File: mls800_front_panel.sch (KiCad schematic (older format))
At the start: 17 parts, among them P5 CONN_02X03, SW10 SW_TACT_LED, SW11 SW_TACT_LED, SW2 SW_TACT_LED, SW3 SW_TACT_LED, SW4 SW_TACT_LED, SW5 SW_TACT_LED, SW6 SW_TACT_LED, SW7 SW_TACT_LED, SW8 SW_TACT_LED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

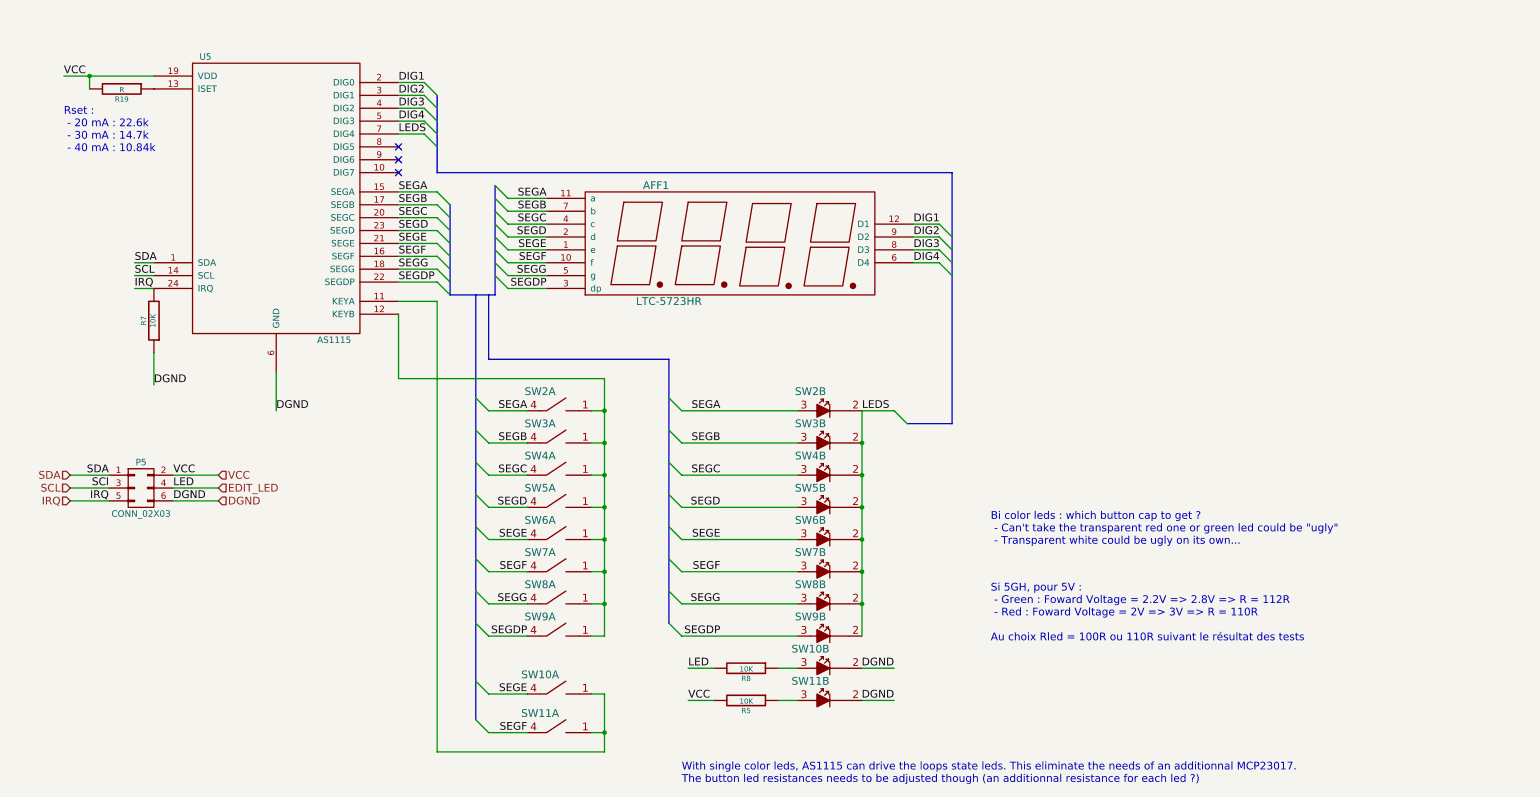
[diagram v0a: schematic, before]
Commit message: MLS800
* splitted schematics for DRC tests
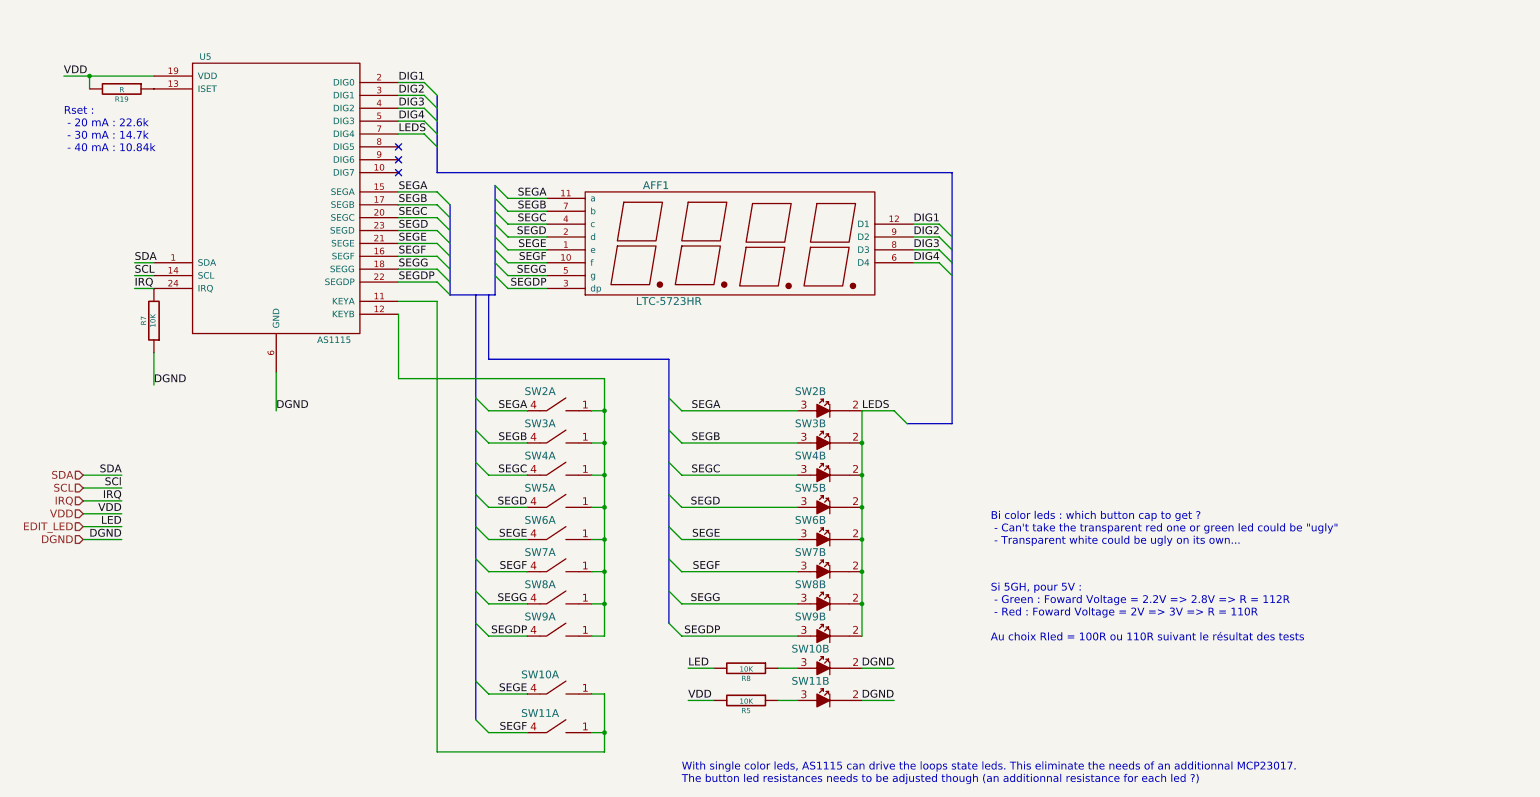
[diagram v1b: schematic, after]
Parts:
- removed P5: CONN_02X03, Pin_Headers:Pin_Header_Straight_2x03, symbol CONN_02X03
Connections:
- net VCC renamed VDD
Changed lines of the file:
@@
 	-1   0    0    1
 $EndComp
-$Comp
-L CONN_02X03 P5
-U 1 1 5497CC76
-P 1450 4150
-F 0 "P5" H 1450 4350 50  0000 C CNN
-F 1 "CONN_02X03" H 1450 3950 50  0000 C CNN
-F 2 "Pin_Headers:Pin_Header_Straight_2x03" H 1450 2950 60  0001 C CNN
-F 3 "" H 1450 2950 60  0000 C CNN
-	1    1450 4150
-	1    0    0    -1
-$EndComp
-Text HLabel 900  4050 0    60   Input ~ 0
-SDA
-Text HLabel 2050 4050 2    60   Input ~ 0
-VCC
-Text HLabel 2050 4250 2    60   Input ~ 0
-DGND
-Text HLabel 2050 4150 2    60   Input ~ 0
-EDIT_LED
-Text HLabel 900  4250 0    60   Input ~ 0
-IRQ
-Text HLabel 900  4150 0    60   Input ~ 0
-SCL
 Wire Wire Line
 	3650 1000 3450 1000
@@
 Wire Wire Line
 	1400 2600 1550 2600
-Wire Wire Line
-	1200 4050 900  4050
-Wire Wire Line
-	900  4150 1200 4150
-Wire Wire Line
-	900  4250 1200 4250
-Wire Wire Line
-	2050 4050 1700 4050
-Wire Wire Line
-	1700 4150 2050 4150
-Wire Wire Line
-	1700 4250 2050 4250
-Text Label 1700 4050 0    60   ~ 0
-VCC
-Text Label 1700 4150 0    60   ~ 0
-LED
-Text Label 1700 4250 0    60   ~ 0
-DGND
-Text Label 1200 4050 2    60   ~ 0
-SDA
-Text Label 1200 4150 2    60   ~ 0
-SCl
-Text Label 1200 4250 2    60   ~ 0
-IRQ
 Connection ~ 1050 950
 Text Label 850  950  0    60   ~ 0
-VCC
+VDD
 Wire Wire Line
 	2500 3250 2500 3550
@@
 	5900 5800 5700 5800
 Text Label 5700 5800 0    60   ~ 0
-VCC
+VDD
 Wire Wire Line
 	7050 5550 7300 5550
@@
 Text Label 7300 5550 2    60   ~ 0
 DGND
+Text Label 1300 4250 2    60   ~ 0
+IRQ
+Text Label 1300 4150 2    60   ~ 0
+SCl
+Text Label 1300 4050 2    60   ~ 0
+SDA
+Text Label 1300 4550 2    60   ~ 0
+DGND
+Text Label 1300 4450 2    60   ~ 0
+LED
+Text Label 1300 4350 2    60   ~ 0
+VDD
+Wire Wire Line
+	1300 4550 1000 4550
+Wire Wire Line
+	1300 4450 1000 4450
+Wire Wire Line
+	1000 4350 1300 4350
+Wire Wire Line
+	1000 4250 1300 4250
+Wire Wire Line
+	1000 4150 1300 4150
+Wire Wire Line
+	1300 4050 1000 4050
+Text HLabel 1000 4150 0    60   Input ~ 0
+SCL
+Text HLabel 1000 4250 0    60   Input ~ 0
+IRQ
+Text HLabel 1000 4450 0    60   Input ~ 0
+EDIT_LED
+Text HLabel 1000 4550 0    60   Input ~ 0
+DGND
+Text HLabel 1000 4350 0    60   Input ~ 0
+VDD
+Text HLabel 1000 4050 0    60   Input ~ 0
+SDA
 $EndSCHEMATC

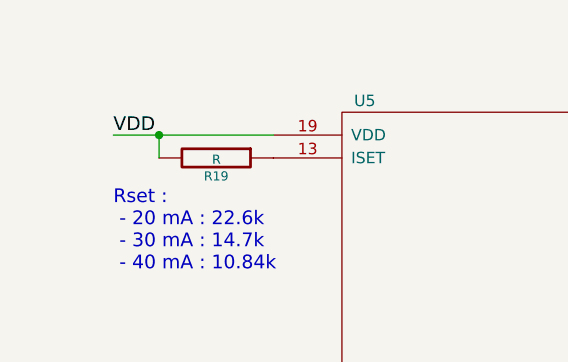
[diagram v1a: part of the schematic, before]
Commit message: MLS800
* rerouting of some part
* added filter cap to each digital part
* added board filter cap
* set 3d shapes for remaining parts (missing custom parts)
* added footprint for small pushbutton
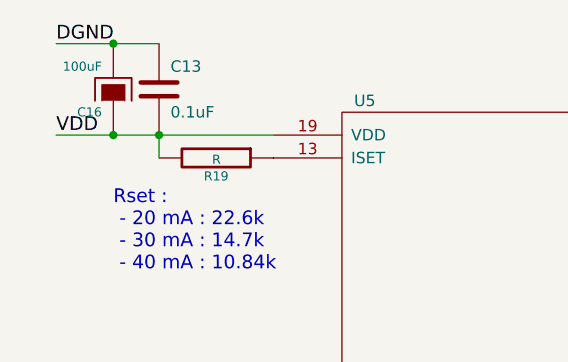
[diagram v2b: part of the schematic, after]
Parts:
- added C13: 0.1uF, Capacitors_SMD:C_0805_HandSoldering, symbol C
- added C16: 100uF, Capacitors_SMD:C_0805_HandSoldering, symbol CAPAPOL
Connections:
- net DGND: now also C13.1, C16.2
- net VDD: now also C13.2, C16.1
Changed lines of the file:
@@
 	1050 1050 1050 950
 Wire Wire Line
-	850  950  1550 950
+	600  950  1550 950
 Wire Wire Line
 	4450 5300 4150 5300
@@
 	1400 2600 1550 2600
 Connection ~ 1050 950
-Text Label 850  950  0    60   ~ 0
+Text Label 600  950  0    60   ~ 0
 VDD
 Wire Wire Line
@@
 Text HLabel 1000 4050 0    60   Input ~ 0
 SDA
+$Comp
+L C C13
+U 1 1 54D9EF4F
+P 1050 750
+F 0 "C13" H 1100 850 50  0000 L CNN
+F 1 "0.1uF" H 1100 650 50  0000 L CNN
+F 2 "Capacitors_SMD:C_0805_HandSoldering" H 1088 600 30  0001 C CNN
+F 3 "" H 1050 750 60  0000 C CNN
+	1    1050 750
+	1    0    0    -1
+$EndComp
+Wire Wire Line
+	600  550  1050 550
+Text Label 600  550  0    60   ~ 0
+DGND
+$Comp
+L CAPAPOL C16
+U 1 1 54DC240E
+P 850 750
+F 0 "C16" H 900 850 40  0000 L CNN
+F 1 "100uF" H 900 650 40  0000 L CNN
+F 2 "Capacitors_SMD:C_0805_HandSoldering" H 950 600 30  0001 C CNN
+F 3 "" H 850 750 300 0000 C CNN
+	1    850  750
+	-1   0    0    1
+$EndComp
+Connection ~ 850  550
+Connection ~ 850  950
 $EndSCHEMATC

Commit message: MLS800
* copper zone clearance
* round drilling holes
*
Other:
- note added: "If using 5V for 5GH : \n - Green : Foward Voltage = 2.2V => 2.8V => R = 112R\n - Red : Foward Voltage = 2V => 3V => R = 110R\n\nAu choix Rled = 100R ou 110R suivant le résultat des tests"
- note removed: "Si 5GH, pour 5V : \n - Green : Foward Voltage = 2.2V => 2.8V => R = 112R\n - Red : Foward Voltage = 2V => 3V => R = 110R\n\nAu choix Rled = 100R ou 110R suivant le résultat des tests"
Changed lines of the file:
@@
 encoding utf-8
 Sheet 3 3
-Title ""
-Date ""
-Rev ""
+Title "MLS800 prototype"
+Date "mercredi 18 février 2015"
+Rev "B"
 Comp ""
 Comment1 ""
@@
 NoConn ~ 3450 1700
 Text Notes 8050 5350 0    60   ~ 0
-Si 5GH, pour 5V : \n - Green : Foward Voltage = 2.2V => 2.8V => R = 112R\n - Red : Foward Voltage = 2V => 3V => R = 110R\n\nAu choix Rled = 100R ou 110R suivant le résultat des tests
+If using 5V for 5GH : \n - Green : Foward Voltage = 2.2V => 2.8V => R = 112R\n - Red : Foward Voltage = 2V => 3V => R = 110R\n\nAu choix Rled = 100R ou 110R suivant le résultat des tests
 $Comp
 L SW_TACT_LED SW10

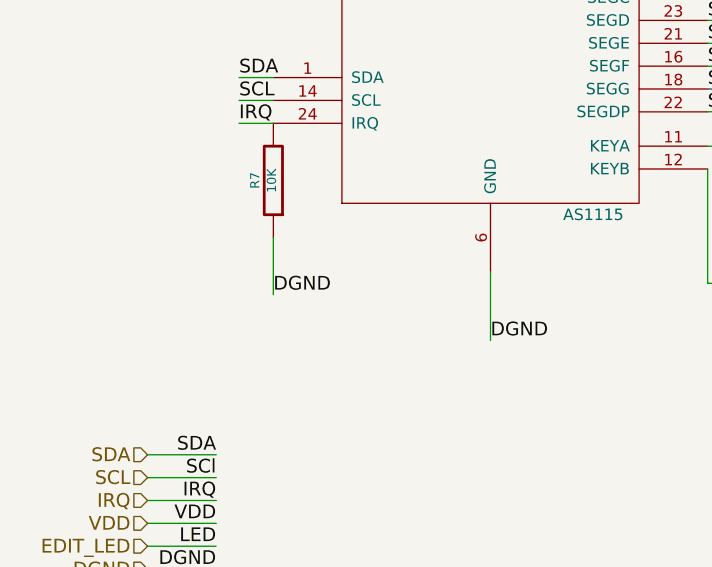
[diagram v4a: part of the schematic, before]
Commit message: Minor PCB adjustements
Fixed R7 tied to ground instead of VCC (needs to be reported on PCB)
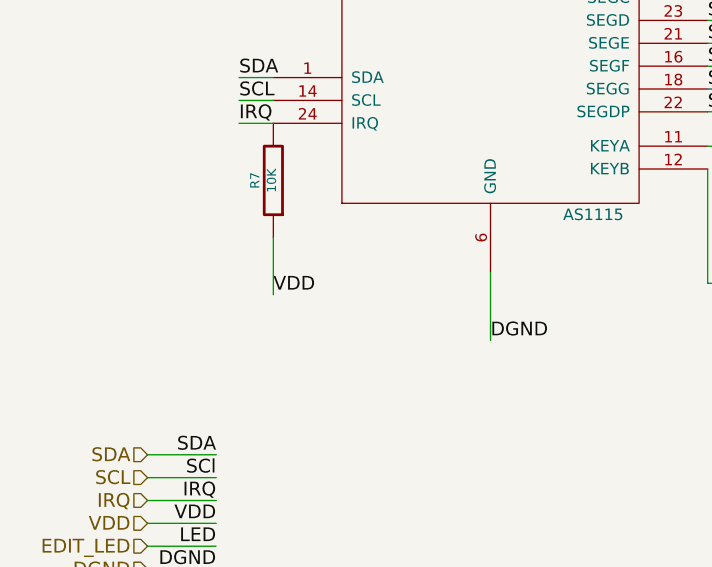
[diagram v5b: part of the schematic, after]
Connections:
- net DGND: no longer R7.1
- net VDD: now also R7.1
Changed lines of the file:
@@
 Text Label 2500 3550 0    60   ~ 0
-DGND
-Text Label 1550 3350 0    60   ~ 0
 DGND
 Wire Wire Line
@@
 Connection ~ 850  550
 Connection ~ 850  950
+Text Label 1550 3350 0    60   ~ 0
+VDD
 $EndSCHEMATC

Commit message: Started components fields assignments
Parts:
- AFF1: Manufacturer (none) -> Lite-On; Manufacturer part number (none) -> LTC-5723HR
- U5: Manufacturer (none) -> ams AG; Manufacturer part number (none) -> AS1115-BSST; Package (none) -> TQFN-24
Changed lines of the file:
@@
 F 2 "Custom-display:LTC-5723" H 5550 2250 60  0001 C CNN
 F 3 "" H 5550 2250 60  0000 C CNN
+F 4 "Lite-On" H 6050 2250 60  0001 C CNN "Manufacturer"
+F 5 "LTC-5723HR" H 6050 2250 60  0001 C CNN "Manufacturer part number"
 	1    6050 2250
 	1    0    0    -1
@@
 F 2 "Housings_SSOP:SSOP-24_3.9x8.7mm_Pitch0.635mm" H 2000 800 50  0001 C CNN
 F 3 "" H 2500 1850 50  0001 C CNN
+F 4 "ams AG" H 2500 1900 60  0001 C CNN "Manufacturer"
+F 5 "AS1115-BSST" H 2500 1900 60  0001 C CNN "Manufacturer part number"
+F 6 "TQFN-24" H 2500 1900 60  0001 C CNN "Package"
 	1    2500 1900
 	1    0    0    -1

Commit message: Components fields assignments
Rerouted relays (set/reset was wired the same way, to reset would have no effect)
Set and reset port have been exchanged to facilitate routing (to be reported on firmware)
Edited relay component
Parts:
- C13, R19, R5, R7, R8: Package (none) -> 0805
- C16: symbol CAPAPOL -> C; Package (none) -> 0805
- SW10, SW11, SW2, SW3, SW5, SW6, SW7, SW8, SW9: Manufacturer (none) -> MEC switches; Manufacturer part number (none) -> 5GSH93582
- SW10, SW11, SW2, SW3, SW4, SW5, SW6, SW7, SW8, SW9: Manufacturer (none) -> MEC switches; Manufacturer part number (none) -> 1ES098
- SW4: Manufacturer (none) -> MEC switches
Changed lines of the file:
@@
 F 2 "Resistors_SMD:R_0805_HandSoldering" V 1230 1050 30  0001 C CNN
 F 3 "" H 1300 1050 30  0000 C CNN
+F 4 "0805" V 1300 1050 60  0001 C CNN "Package"
 	1    1300 1050
 	0    1    1    0
@@
 F 2 "Custom-device:MEC-5G" H 4750 3550 60  0001 C CNN
 F 3 "" H 4750 3550 60  0000 C CNN
+F 4 "MEC switches" H 4750 3550 60  0001 C CNN "Manufacturer"
+F 5 "5GSH93582" H 4750 3550 60  0001 C CNN "Manufacturer part number"
 	1    4750 3550
 	1    0    0    -1
@@
 F 2 "Custom-device:MEC-5G" H 4750 3800 60  0001 C CNN
 F 3 "" H 4750 3800 60  0000 C CNN
+F 4 "MEC switches" H 4750 3800 60  0001 C CNN "Manufacturer"
+F 5 "5GSH93582" H 4750 3800 60  0001 C CNN "Manufacturer part number"
 	1    4750 3800
 	1    0    0    -1
@@
 F 2 "Custom-device:MEC-5G" H 4750 4050 60  0001 C CNN
 F 3 "" H 4750 4050 60  0000 C CNN
+F 4 "MEC switches" H 4750 4050 60  0001 C CNN "Manufacturer"
 	1    4750 4050
 	1    0    0    -1
@@
 F 2 "Custom-device:MEC-5G" H 4750 4300 60  0001 C CNN
 F 3 "" H 4750 4300 60  0000 C CNN
+F 4 "MEC switches" H 4750 4300 60  0001 C CNN "Manufacturer"
+F 5 "5GSH93582" H 4750 4300 60  0001 C CNN "Manufacturer part number"
 	1    4750 4300
 	1    0    0    -1
@@
 F 2 "Custom-device:MEC-5G" H 4750 4550 60  0001 C CNN
 F 3 "" H 4750 4550 60  0000 C CNN
+F 4 "MEC switches" H 4750 4550 60  0001 C CNN "Manufacturer"
+F 5 "5GSH93582" H 4750 4550 60  0001 C CNN "Manufacturer part number"
 	1    4750 4550
 	1    0    0    -1
@@
 F 2 "Custom-device:MEC-5G" H 4750 4800 60  0001 C CNN
 F 3 "" H 4750 4800 60  0000 C CNN
+F 4 "MEC switches" H 4750 4800 60  0001 C CNN "Manufacturer"
+F 5 "5GSH93582" H 4750 4800 60  0001 C CNN "Manufacturer part number"
 	1    4750 4800
 	1    0    0    -1
@@
 F 2 "Custom-device:MEC-5G" H 4750 5050 60  0001 C CNN
 F 3 "" H 4750 5050 60  0000 C CNN
+F 4 "MEC switches" H 4750 5050 60  0001 C CNN "Manufacturer"
+F 5 "5GSH93582" H 4750 5050 60  0001 C CNN "Manufacturer part number"
 	1    4750 5050
 	1    0    0    -1
@@
 F 2 "Custom-device:MEC-5G" H 4750 5300 60  0001 C CNN
 F 3 "" H 4750 5300 60  0000 C CNN
+F 4 "MEC switches" H 4750 5300 60  0001 C CNN "Manufacturer"
+F 5 "5GSH93582" H 4750 5300 60  0001 C CNN "Manufacturer part number"
 	1    4750 5300
 	1    0    0    -1
@@
 F 2 "Custom-device:MEC-5G" H 6850 3550 60  0001 C CNN
 F 3 "" H 6850 3550 60  0000 C CNN
+F 4 "MEC switches" H 6850 3550 60  0001 C CNN "Manufacturer"
+F 5 "1ES098" H 6850 3550 60  0001 C CNN "Manufacturer part number"
 	2    6850 3550
 	1    0    0    -1
@@
 F 2 "Custom-device:MEC-5G" H 6850 3800 60  0001 C CNN
 F 3 "" H 6850 3800 60  0000 C CNN
+F 4 "MEC switches" H 6850 3800 60  0001 C CNN "Manufacturer"
+F 5 "1ES098" H 6850 3800 60  0001 C CNN "Manufacturer part number"
 	2    6850 3800
 	1    0    0    -1
@@
 F 2 "Custom-device:MEC-5G" H 6850 4050 60  0001 C CNN
 F 3 "" H 6850 4050 60  0000 C CNN
+F 4 "MEC switches" H 6850 4050 60  0001 C CNN "Manufacturer"
+F 5 "1ES098" H 6850 4050 60  0001 C CNN "Manufacturer part number"
 	2    6850 4050
 	1    0    0    -1
@@
 F 2 "Custom-device:MEC-5G" H 6850 4300 60  0001 C CNN
 F 3 "" H 6850 4300 60  0000 C CNN
+F 4 "MEC switches" H 6850 4300 60  0001 C CNN "Manufacturer"
+F 5 "1ES098" H 6850 4300 60  0001 C CNN "Manufacturer part number"
 	2    6850 4300
 	1    0    0    -1
@@
 F 2 "Custom-device:MEC-5G" H 6850 4550 60  0001 C CNN
 F 3 "" H 6850 4550 60  0000 C CNN
+F 4 "MEC switches" H 6850 4550 60  0001 C CNN "Manufacturer"
+F 5 "1ES098" H 6850 4550 60  0001 C CNN "Manufacturer part number"
 	2    6850 4550
 	1    0    0    -1
@@
 F 2 "Custom-device:MEC-5G" H 6850 4800 60  0001 C CNN
 F 3 "" H 6850 4800 60  0000 C CNN
+F 4 "MEC switches" H 6850 4800 60  0001 C CNN "Manufacturer"
+F 5 "1ES098" H 6850 4800 60  0001 C CNN "Manufacturer part number"
 	2    6850 4800
 	1    0    0    -1
@@
 F 2 "Custom-device:MEC-5G" H 6850 5050 60  0001 C CNN
 F 3 "" H 6850 5050 60  0000 C CNN
+F 4 "MEC switches" H 6850 5050 60  0001 C CNN "Manufacturer"
+F 5 "1ES098" H 6850 5050 60  0001 C CNN "Manufacturer part number"
 	2    6850 5050
 	1    0    0    -1
@@
 F 2 "Custom-device:MEC-5G" H 6850 5300 60  0001 C CNN
 F 3 "" H 6850 5300 60  0000 C CNN
+F 4 "MEC switches" H 6850 5300 60  0001 C CNN "Manufacturer"
+F 5 "1ES098" H 6850 5300 60  0001 C CNN "Manufacturer part number"
 	2    6850 5300
 	1    0    0    -1
@@
 F 2 "Custom-device:MEC-5G" H 4750 5750 60  0001 C CNN
 F 3 "" H 4750 5750 60  0000 C CNN
+F 4 "MEC switches" H 4750 5750 60  0001 C CNN "Manufacturer"
+F 5 "5GSH93582" H 4750 5750 60  0001 C CNN "Manufacturer part number"
 	1    4750 5750
 	1    0    0    -1
@@
 F 2 "Custom-device:MEC-5G" H 4750 6050 60  0001 C CNN
 F 3 "" H 4750 6050 60  0000 C CNN
+F 4 "MEC switches" H 4750 6050 60  0001 C CNN "Manufacturer"
+F 5 "5GSH93582" H 4750 6050 60  0001 C CNN "Manufacturer part number"
 	1    4750 6050
 	1    0    0    -1
@@
 F 2 "Resistors_SMD:R_0805_HandSoldering" H 6080 5550 30  0001 C CNN
 F 3 "" H 6150 5550 30  0000 C CNN
+F 4 "0805" V 6150 5550 60  0001 C CNN "Package"
 	1    6150 5550
 	0    1    1    0
@@
 F 2 "Custom-device:MEC-5G" H 6850 5550 60  0001 C CNN
 F 3 "" H 6850 5550 60  0000 C CNN
+F 4 "MEC switches" H 6850 5550 60  0001 C CNN "Manufacturer"
+F 5 "1ES098" H 6850 5550 60  0001 C CNN "Manufacturer part number"
 	2    6850 5550
 	1    0    0    -1
@@
 F 2 "Resistors_SMD:R_0805_HandSoldering" H 6080 5800 30  0001 C CNN
 F 3 "" H 6150 5800 30  0000 C CNN
+F 4 "0805" V 6150 5800 60  0001 C CNN "Package"
 	1    6150 5800
 	0    1    1    0
@@
 F 2 "Custom-device:MEC-5G" H 6850 5800 60  0001 C CNN
 F 3 "" H 6850 5800 60  0000 C CNN
+F 4 "MEC switches" H 6850 5800 60  0001 C CNN "Manufacturer"
+F 5 "1ES098" H 6850 5800 60  0001 C CNN "Manufacturer part number"
 	2    6850 5800
 	1    0    0    -1
@@
 F 2 "Resistors_SMD:R_0805_HandSoldering" V 1480 2850 30  0001 C CNN
 F 3 "" H 1550 2850 30  0000 C CNN
+F 4 "0805" V 1550 2850 60  0001 C CNN "Package"
 	1    1550 2850
 	-1   0    0    1
@@
 F 2 "Capacitors_SMD:C_0805_HandSoldering" H 1088 600 30  0001 C CNN
 F 3 "" H 1050 750 60  0000 C CNN
+F 4 "0805" H 1050 750 60  0001 C CNN "Package"
 	1    1050 750
 	1    0    0    -1
@@
 DGND
 $Comp
-L CAPAPOL C16
+L C C16
 U 1 1 54DC240E
 P 850 750
@@
 F 2 "Capacitors_SMD:C_0805_HandSoldering" H 950 600 30  0001 C CNN
 F 3 "" H 850 750 300 0000 C CNN
+F 4 "0805" H 850 750 60  0001 C CNN "Package"
 	1    850  750
 	-1   0    0    1

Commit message: Components fields assignments
Silkscreen dots marker
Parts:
- R19: value R -> 23.6k
- R5, R8: value 10K -> 250R
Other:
- note added: "Rset : \n - 20 mA : 23.6k\n - 30 mA : 15.4k\n - 40 mA : 11.35k"
- note removed: "Bi color leds : which button cap to get ?\n - Can't take the transparent red one or green led could be "ugly"\n - Transparent white could be ugly on its own..."
- note removed: "Rset : \n - 20 mA : 22.6k\n - 30 mA : 14.7k\n - 40 mA : 10.84k"
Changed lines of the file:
@@
 P 1300 1050
 F 0 "R19" V 1380 1050 40  0000 C CNN
-F 1 "R" V 1307 1051 40  0000 C CNN
+F 1 "23.6k" V 1307 1051 40  0000 C CNN
 F 2 "Resistors_SMD:R_0805_HandSoldering" V 1230 1050 30  0001 C CNN
 F 3 "" H 1300 1050 30  0000 C CNN
@@
 $EndComp
 Text Notes 850  1550 0    60   ~ 0
-Rset : \n - 20 mA : 22.6k\n - 30 mA : 14.7k\n - 40 mA : 10.84k
-Text Notes 8050 4600 0    60   ~ 0
-Bi color leds : which button cap to get ?\n - Can't take the transparent red one or green led could be "ugly"\n - Transparent white could be ugly on its own...
+Rset : \n - 20 mA : 23.6k\n - 30 mA : 15.4k\n - 40 mA : 11.35k
 Text Notes 5650 6450 0    60   ~ 0
 With single color leds, AS1115 can drive the loops state leds. This eliminate the needs of an additionnal MCP23017.\nThe button led resistances needs to be adjusted though (an additionnal resistance for each led ?)
@@
 P 6150 5550
 F 0 "R8" V 6230 5550 40  0000 C CNN
-F 1 "10K" V 6157 5551 40  0000 C CNN
+F 1 "250R" V 6157 5551 40  0000 C CNN
 F 2 "Resistors_SMD:R_0805_HandSoldering" H 6080 5550 30  0001 C CNN
 F 3 "" H 6150 5550 30  0000 C CNN
@@
 P 6150 5800
 F 0 "R5" V 6230 5800 40  0000 C CNN
-F 1 "10K" V 6157 5801 40  0000 C CNN
+F 1 "250R" V 6157 5801 40  0000 C CNN
 F 2 "Resistors_SMD:R_0805_HandSoldering" H 6080 5800 30  0001 C CNN
 F 3 "" H 6150 5800 30  0000 C CNN
